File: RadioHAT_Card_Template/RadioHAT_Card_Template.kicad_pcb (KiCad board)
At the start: 2 copper layers, 30 x 51 mm, 1 part

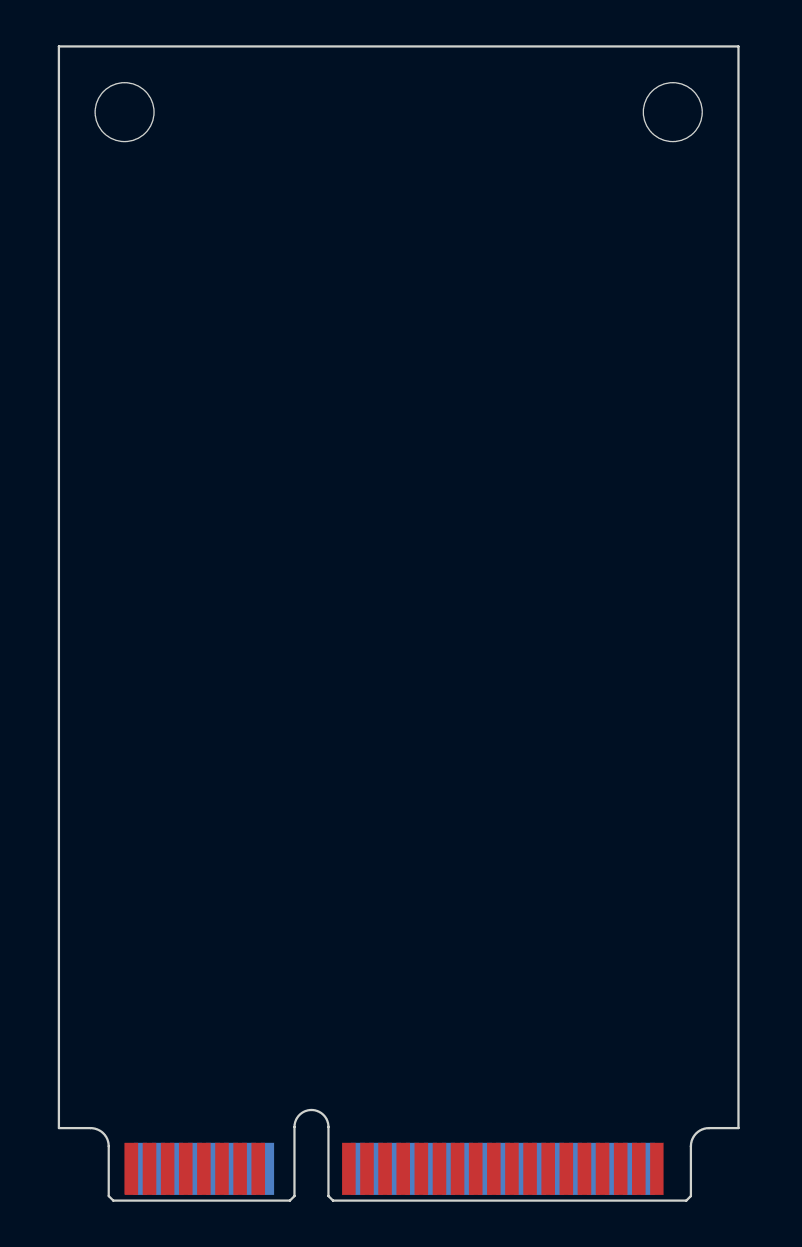
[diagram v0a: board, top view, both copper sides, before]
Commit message: Fix errors in template
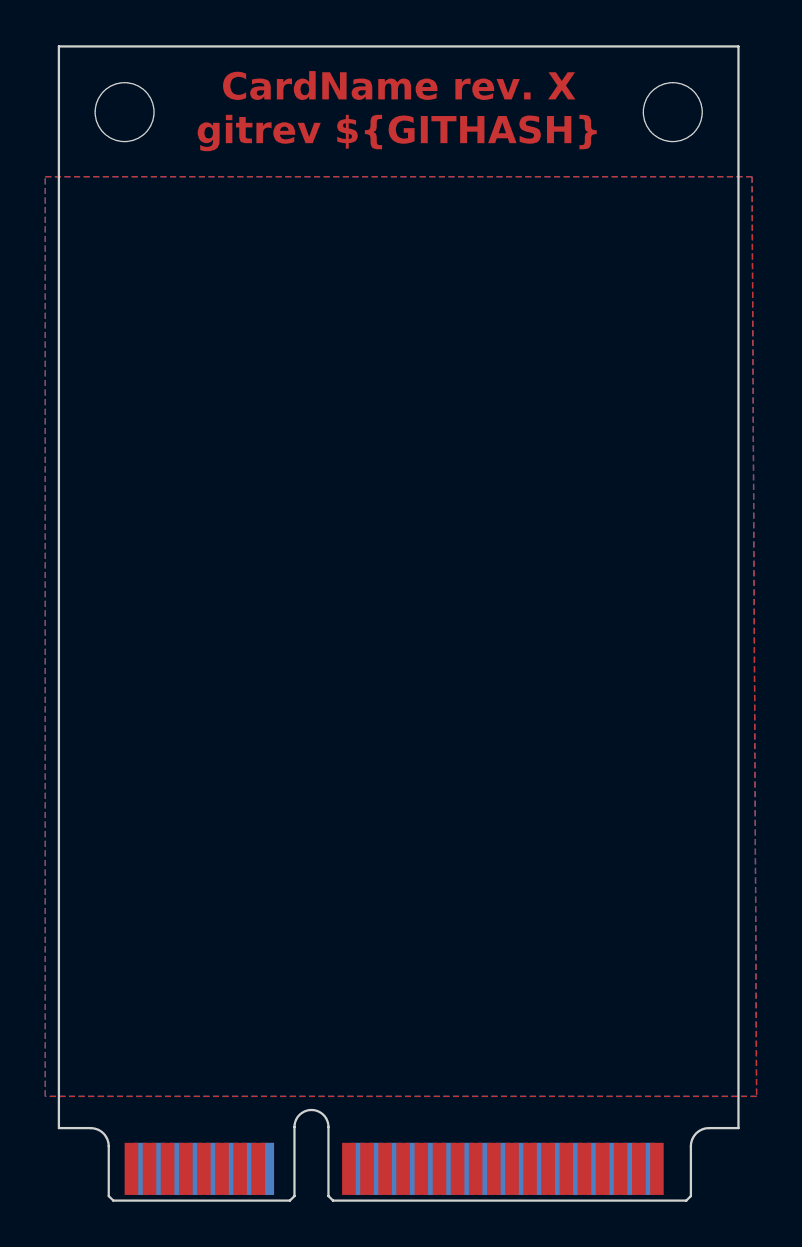
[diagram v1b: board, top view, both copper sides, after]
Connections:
- J1 pad 20: unconnected-(J1-NSS1-Pad20) -> NSS1
- J1 pad 51: unconnected-(J1-NSS0-Pad51) -> NSS0
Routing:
- added copper zone on B.Cu, net GND
- added copper zone on F.Cu, net GND
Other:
- board text added: "CardName rev. X gitrev ${GITHASH}"
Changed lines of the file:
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@@
 		)
 	)
+	(property "GITHASH" "GITHASH")
 	(net 0 "")
 	(net 1 "+5V")
 	(net 2 "MISO")
 	(net 3 "RST0")
-	(net 4 "unconnected-(J1-NSS0-Pad51)")
+	(net 4 "NSS0")
 	(net 5 "GPIO0")
 	(net 6 "+3V3")
@@
 	(net 16 "unconnected-(J1-USB_D--Pad36)")
 	(net 17 "GPIO1")
-	(net 18 "unconnected-(J1-NSS1-Pad20)")
+	(net 18 "NSS1")
 	(net 19 "unconnected-(J1-LED1-Pad44)")
 	(net 20 "unconnected-(J1-LED0-Pad42)")
@@
 			(size 2.3 0.6)
 			(layers "B.Cu" "B.Mask" "B.Paste")
-			(net 18 "unconnected-(J1-NSS1-Pad20)")
+			(net 18 "NSS1")
 			(pinfunction "NSS1")
 			(pintype "bidirectional")
@@
 			(size 2.3 0.6)
 			(layers "F.Cu" "F.Mask" "F.Paste")
-			(net 4 "unconnected-(J1-NSS0-Pad51)")
+			(net 4 "NSS0")
 			(pinfunction "NSS0")
 			(pintype "bidirectional")
@@
 		)
 		(embedded_fonts no)
+	)
+	(gr_text "CardName rev. X\ngitrev ${GITHASH}"
+		(at 150.4 76 0)
+		(layer "F.Cu")
+		(effects
+			(font
+				(size 1.2 1.2)
+				(thickness 0.25)
+				(bold yes)
+			)
+		)
 	)
 	(dimension
@@
 			)
 		)
+	)
+	(zone
+		(net 8)
+		(net_name "GND")
+		(layers "F.Cu" "B.Cu")
+		(hatch edge 0.5)
+		(connect_pads
+			(clearance 0.5)
+		)
+		(min_thickness 0.25)
+		(filled_areas_thickness no)
+		(fill yes
+			(thermal_gap 0.5)
+			(thermal_bridge_width 0.5)
+		)
+		(polygon
+			(pts
+				(xy 134.8 79) (xy 166 79) (xy 166.2 119.6) (xy 134.8 119.6)
+			)
+		)
